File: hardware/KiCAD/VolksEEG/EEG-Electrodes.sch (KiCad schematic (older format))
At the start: 33 parts, among them J1 Conn_02x13_Odd_Even

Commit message: Updating analogue inputs to the referential montage and connected a few ADS1299 pins.
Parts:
- removed C11, C? (x14): 4.7n, Capacitor_SMD:C_0603_1608Metric_Pad1.08x0.95mm_HandSolder, symbol Device:C
- removed R? (x8): 4.99k, Resistor_SMD:R_0603_1608Metric_Pad0.98x0.95mm_HandSolder, symbol Device:R
- added C? (x8): 4.7n, Capacitor_SMD:C_0603_1608Metric_Pad1.08x0.95mm_HandSolder, symbol Device:C
- added R? (x3): 4.99k, Resistor_SMD:R_0603_1608Metric_Pad0.98x0.95mm_HandSolder, symbol Device:R
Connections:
- net labels added: AIN1, AIN2, AIN3, AIN4, AIN5, AIN6, AIN7, AIN8, BIAS_INV, BIAS_OUT, REF
- net labels removed: AIN1N, AIN1P, AIN2N, AIN2P, AIN3N, AIN3P, AIN4N, AIN4P, AIN5N, AIN5P, AIN6N, AIN6P, AIN7N, AIN7P, AIN8N, AIN8P
- wire segments 116 -> 74
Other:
- moved on the sheet: C10, R1, R?

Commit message: Updated names of heirarchical pins, finished referential montage configuration, added filter cap to ADS_nRST line, started putting ADS1299 gpios to a header.
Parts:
- removed J1: Conn_02x13_Odd_Even, Connector_PinHeader_2.54mm:PinHeader_2x13_P2.54mm_Vertical, symbol Connector_Generic:Conn_02x13_Odd_Even
- added J?: Conn_01x10, symbol Connector_Generic:Conn_01x10
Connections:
- net labels removed: ELEC1N, ELEC1P, ELEC2N, ELEC2P, ELEC3N, ELEC3P, ELEC4N, ELEC4P, ELEC5N, ELEC5P, ELEC6N, ELEC6P, ELEC7N, ELEC7P, ELEC8N, ELEC8P, GNDA, VDDA, VSSA
- wire segments 74 -> 76
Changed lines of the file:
@@
 AIN8
-$Comp
-L Connector_Generic:Conn_02x13_Odd_Even J1
-U 1 1 61659FCB
-P 8600 3450
-F 0 "J1" H 8650 2625 50  0000 C CNN
-F 1 "Conn_02x13_Odd_Even" H 8650 2716 50  0000 C CNN
-F 2 "Connector_PinHeader_2.54mm:PinHeader_2x13_P2.54mm_Vertical" H 8600 3450 50  0001 C CNN
-F 3 "~" H 8600 3450 50  0001 C CNN
-	1    8600 3450
-	-1   0    0    1
-$EndComp
-$Comp
-L power:VDDA #PWR036
-U 1 1 6165D31B
-P 7950 2750
-F 0 "#PWR036" H 7950 2600 50  0001 C CNN
-F 1 "VDDA" H 7965 2923 50  0000 C CNN
-F 2 "" H 7950 2750 50  0001 C CNN
-F 3 "" H 7950 2750 50  0001 C CNN
-	1    7950 2750
-	1    0    0    -1
-$EndComp
-$Comp
-L power:VDDA #PWR039
-U 1 1 6165DEAF
-P 9150 2750
-F 0 "#PWR039" H 9150 2600 50  0001 C CNN
-F 1 "VDDA" H 9165 2923 50  0000 C CNN
-F 2 "" H 9150 2750 50  0001 C CNN
-F 3 "" H 9150 2750 50  0001 C CNN
-	1    9150 2750
-	1    0    0    -1
-$EndComp
-$Comp
-L power:VSSA #PWR038
-U 1 1 6165EC47
-P 8800 4150
-F 0 "#PWR038" H 8800 4000 50  0001 C CNN
-F 1 "VSSA" H 8815 4323 50  0000 C CNN
-F 2 "" H 8800 4150 50  0001 C CNN
-F 3 "" H 8800 4150 50  0001 C CNN
-	1    8800 4150
-	-1   0    0    1
-$EndComp
-$Comp
-L power:VSSA #PWR037
-U 1 1 6165FAEA
-P 8300 4150
-F 0 "#PWR037" H 8300 4000 50  0001 C CNN
-F 1 "VSSA" H 8315 4323 50  0000 C CNN
-F 2 "" H 8300 4150 50  0001 C CNN
-F 3 "" H 8300 4150 50  0001 C CNN
-	1    8300 4150
-	-1   0    0    1
-$EndComp
-Wire Wire Line
-	9200 2950 8800 2950
-Wire Wire Line
-	8800 2850 9150 2850
-Wire Wire Line
-	9150 2850 9150 2750
-Wire Wire Line
-	8300 2850 7950 2850
-Wire Wire Line
-	7950 2850 7950 2750
-Wire Wire Line
-	7900 2950 8300 2950
-Wire Wire Line
-	8300 4150 8300 4050
-Wire Wire Line
-	8800 4050 8800 4150
-Wire Wire Line
-	7950 3050 8300 3050
-Wire Wire Line
-	7950 3150 8300 3150
-Wire Wire Line
-	7950 3250 8300 3250
-Wire Wire Line
-	7950 3350 8300 3350
-Wire Wire Line
-	7950 3450 8300 3450
-Wire Wire Line
-	7950 3550 8300 3550
-Wire Wire Line
-	7950 3650 8300 3650
-Wire Wire Line
-	7950 3750 8300 3750
-Wire Wire Line
-	7950 3850 8300 3850
-Wire Wire Line
-	7950 3950 8300 3950
-Wire Wire Line
-	9150 3950 8800 3950
-Wire Wire Line
-	9150 3850 8800 3850
-Wire Wire Line
-	9150 3750 8800 3750
-Wire Wire Line
-	9150 3650 8800 3650
-Wire Wire Line
-	9150 3550 8800 3550
-Wire Wire Line
-	9150 3450 8800 3450
-Wire Wire Line
-	9150 3350 8800 3350
-Wire Wire Line
-	9150 3250 8800 3250
-Wire Wire Line
-	9150 3150 8800 3150
-Wire Wire Line
-	9150 3050 8800 3050
-Text Label 7950 3850 0    50   ~ 0
-ELEC1N
-Text Label 8850 3850 0    50   ~ 0
-ELEC1P
-Entry Wire Line
-	7850 3250 7950 3150
-Entry Wire Line
-	7850 3150 7950 3050
-Entry Wire Line
-	7850 3350 7950 3250
-Entry Wire Line
-	7850 3450 7950 3350
-Entry Wire Line
-	7850 3550 7950 3450
-Entry Wire Line
-	7850 3650 7950 3550
-Entry Wire Line
-	7850 3750 7950 3650
-Entry Wire Line
-	7850 3850 7950 3750
-Entry Wire Line
-	7850 3950 7950 3850
-Entry Wire Line
-	7850 4050 7950 3950
-Entry Wire Line
-	9250 3150 9150 3050
-Entry Wire Line
-	9250 3250 9150 3150
-Entry Wire Line
-	9250 3350 9150 3250
-Entry Wire Line
-	9250 3450 9150 3350
-Entry Wire Line
-	9250 3550 9150 3450
-Entry Wire Line
-	9250 3650 9150 3550
-Entry Wire Line
-	9250 3750 9150 3650
-Entry Wire Line
-	9250 3850 9150 3750
-Entry Wire Line
-	9250 3950 9150 3850
-Entry Wire Line
-	9250 4050 9150 3950
-Text Label 7950 3750 0    50   ~ 0
-ELEC2N
-Text Label 8850 3750 0    50   ~ 0
-ELEC2P
-Text Label 7950 3650 0    50   ~ 0
-ELEC3N
-Text Label 8850 3650 0    50   ~ 0
-ELEC3P
-Text Label 7950 3550 0    50   ~ 0
-ELEC4N
-Text Label 8850 3550 0    50   ~ 0
-ELEC4P
-Text Label 7950 3450 0    50   ~ 0
-ELEC5N
-Text Label 8850 3450 0    50   ~ 0
-ELEC5P
-Text Label 7950 3350 0    50   ~ 0
-ELEC6N
-Text Label 8850 3350 0    50   ~ 0
-ELEC6P
-Text Label 7950 3250 0    50   ~ 0
-ELEC7N
-Text Label 8850 3250 0    50   ~ 0
-ELEC7P
-Text Label 7950 3150 0    50   ~ 0
-ELEC8N
-Text Label 8850 3150 0    50   ~ 0
-ELEC8P
 $Comp
 L Device:R R?
@@
 	1    5800 3950
 	0    1    1    0
-$EndComp
-$Comp
-L power:GNDA #PWR?
-U 1 1 617E796B
-P 7900 2950
-F 0 "#PWR?" H 7900 2700 50  0001 C CNN
-F 1 "GNDA" H 7905 2777 50  0000 C CNN
-F 2 "" H 7900 2950 50  0001 C CNN
-F 3 "" H 7900 2950 50  0001 C CNN
-	1    7900 2950
-	0    1    1    0
-$EndComp
-$Comp
-L power:GNDA #PWR?
-U 1 1 617EC38A
-P 9200 2950
-F 0 "#PWR?" H 9200 2700 50  0001 C CNN
-F 1 "GNDA" H 9205 2777 50  0000 C CNN
-F 2 "" H 9200 2950 50  0001 C CNN
-F 3 "" H 9200 2950 50  0001 C CNN
-	1    9200 2950
-	0    -1   -1   0
 $EndComp
 Text HLabel 2200 4600 0    50   Output ~ 0
@@
 	5650 5200 3100 5200
 Connection ~ 3100 5200
+$Comp
+L Connector_Generic:Conn_01x10 J?
+U 1 1 61B400D9
+P 8500 3150
+F 0 "J?" H 8580 3142 50  0000 L CNN
+F 1 "Conn_01x10" H 8580 3051 50  0000 L CNN
+F 2 "" H 8500 3150 50  0001 C CNN
+F 3 "~" H 8500 3150 50  0001 C CNN
+	1    8500 3150
+	1    0    0    -1
+$EndComp
+Wire Wire Line
+	5950 1850 7750 1850
+Wire Wire Line
+	7750 1850 7750 2750
+Wire Wire Line
+	7750 2750 8300 2750
+Wire Wire Line
+	5950 2150 7600 2150
+Wire Wire Line
+	7600 2150 7600 2850
+Wire Wire Line
+	7600 2850 8300 2850
+Wire Wire Line
+	7450 2950 7450 2450
+Wire Wire Line
+	7450 2450 5950 2450
+Wire Wire Line
+	5950 2750 7300 2750
+Wire Wire Line
+	7300 2750 7300 3050
+Wire Wire Line
+	7300 3050 8300 3050
+Wire Wire Line
+	8300 3150 7150 3150
+Wire Wire Line
+	7150 3150 7150 3050
+Wire Wire Line
+	7150 3050 5950 3050
+Wire Wire Line
+	7450 2950 8300 2950
+Wire Wire Line
+	5950 3350 7150 3350
+Wire Wire Line
+	7150 3350 7150 3250
+Wire Wire Line
+	7150 3250 8300 3250
+Wire Wire Line
+	8300 3350 7300 3350
+Wire Wire Line
+	7300 3650 5950 3650
+Wire Wire Line
+	7300 3350 7300 3650
+Wire Wire Line
+	5950 3950 7450 3950
+Wire Wire Line
+	7450 3950 7450 3450
+Wire Wire Line
+	7450 3450 8300 3450
+Wire Wire Line
+	5950 4600 7600 4600
+Wire Wire Line
+	7600 4600 7600 3550
+Wire Wire Line
+	7600 3550 8300 3550
+Wire Wire Line
+	5950 5200 7750 5200
+Wire Wire Line
+	7750 5200 7750 3650
+Wire Wire Line
+	7750 3650 8300 3650
 $EndSCHEMATC

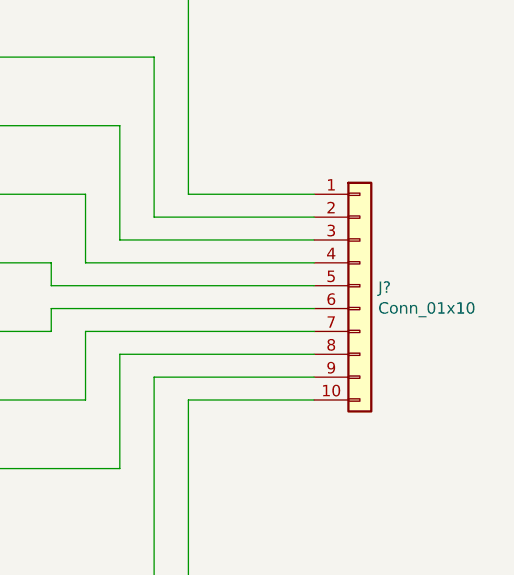
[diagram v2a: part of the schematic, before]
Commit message: Added custom power symbols for non isolated power. Seperated Analogue and digital supplies. finished putting the ADS1299 GPIOs to a header.
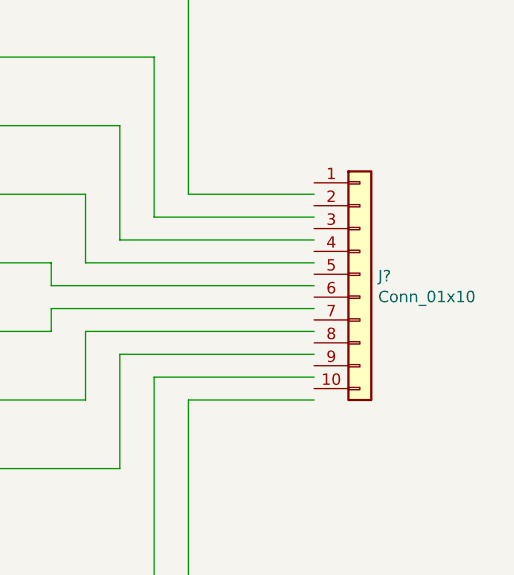
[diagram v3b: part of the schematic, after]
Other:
- moved on the sheet: J?
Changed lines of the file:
@@
 L Connector_Generic:Conn_01x10 J?
 U 1 1 61B400D9
-P 8500 3150
-F 0 "J?" H 8580 3142 50  0000 L CNN
-F 1 "Conn_01x10" H 8580 3051 50  0000 L CNN
-F 2 "" H 8500 3150 50  0001 C CNN
-F 3 "~" H 8500 3150 50  0001 C CNN
-	1    8500 3150
+P 8500 3100
+F 0 "J?" H 8580 3092 50  0000 L CNN
+F 1 "Conn_01x10" H 8580 3001 50  0000 L CNN
+F 2 "" H 8500 3100 50  0001 C CNN
+F 3 "~" H 8500 3100 50  0001 C CNN
+	1    8500 3100
 	1    0    0    -1
 $EndComp

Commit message: Added debugging bits to more schematic sheets.
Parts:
- C10, C? (x8): value 4.7n -> 33n
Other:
- note added: "RC values chosen to give roughly 1KHz -3dB point"
- moved on the sheet: J?
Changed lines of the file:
@@
 $Descr A4 11693 8268
 encoding utf-8
-Sheet 6 6
+Sheet 4 6
 Title ""
 Date ""
@@
 P 2500 4350
 F 0 "C10" H 2615 4396 50  0000 L CNN
-F 1 "4.7n" H 2615 4305 50  0000 L CNN
+F 1 "33n" H 2615 4305 50  0000 L CNN
 F 2 "Capacitor_SMD:C_0603_1608Metric_Pad1.08x0.95mm_HandSolder" H 2538 4200 50  0001 C CNN
 F 3 "~" H 2500 4350 50  0001 C CNN
@@
 P 2900 4350
 F 0 "C?" H 3015 4396 50  0000 L CNN
-F 1 "4.7n" H 3015 4305 50  0000 L CNN
+F 1 "33n" H 3015 4305 50  0000 L CNN
 F 2 "Capacitor_SMD:C_0603_1608Metric_Pad1.08x0.95mm_HandSolder" H 2938 4200 50  0001 C CNN
 F 3 "~" H 2900 4350 50  0001 C CNN
@@
 P 3300 4350
 F 0 "C?" H 3415 4396 50  0000 L CNN
-F 1 "4.7n" H 3415 4305 50  0000 L CNN
+F 1 "33n" H 3415 4305 50  0000 L CNN
 F 2 "Capacitor_SMD:C_0603_1608Metric_Pad1.08x0.95mm_HandSolder" H 3338 4200 50  0001 C CNN
 F 3 "~" H 3300 4350 50  0001 C CNN
@@
 P 3700 4350
 F 0 "C?" H 3815 4396 50  0000 L CNN
-F 1 "4.7n" H 3815 4305 50  0000 L CNN
+F 1 "33n" H 3815 4305 50  0000 L CNN
 F 2 "Capacitor_SMD:C_0603_1608Metric_Pad1.08x0.95mm_HandSolder" H 3738 4200 50  0001 C CNN
 F 3 "~" H 3700 4350 50  0001 C CNN
@@
 P 4100 4350
 F 0 "C?" H 4215 4396 50  0000 L CNN
-F 1 "4.7n" H 4215 4305 50  0000 L CNN
+F 1 "33n" H 4215 4305 50  0000 L CNN
 F 2 "Capacitor_SMD:C_0603_1608Metric_Pad1.08x0.95mm_HandSolder" H 4138 4200 50  0001 C CNN
 F 3 "~" H 4100 4350 50  0001 C CNN
@@
 P 4500 4350
 F 0 "C?" H 4615 4396 50  0000 L CNN
-F 1 "4.7n" H 4615 4305 50  0000 L CNN
+F 1 "33n" H 4615 4305 50  0000 L CNN
 F 2 "Capacitor_SMD:C_0603_1608Metric_Pad1.08x0.95mm_HandSolder" H 4538 4200 50  0001 C CNN
 F 3 "~" H 4500 4350 50  0001 C CNN
@@
 P 4950 4350
 F 0 "C?" H 5065 4396 50  0000 L CNN
-F 1 "4.7n" H 5065 4305 50  0000 L CNN
+F 1 "33n" H 5065 4305 50  0000 L CNN
 F 2 "Capacitor_SMD:C_0603_1608Metric_Pad1.08x0.95mm_HandSolder" H 4988 4200 50  0001 C CNN
 F 3 "~" H 4950 4350 50  0001 C CNN
@@
 P 5350 4350
 F 0 "C?" H 5465 4396 50  0000 L CNN
-F 1 "4.7n" H 5465 4305 50  0000 L CNN
+F 1 "33n" H 5465 4305 50  0000 L CNN
 F 2 "Capacitor_SMD:C_0603_1608Metric_Pad1.08x0.95mm_HandSolder" H 5388 4200 50  0001 C CNN
 F 3 "~" H 5350 4350 50  0001 C CNN
@@
 AR Path="/615BA110/61ADFC6A" Ref="C?"  Part="1"
 F 0 "C?" H 2865 5096 50  0000 L CNN
-F 1 "4.7n" H 2865 5005 50  0000 L CNN
+F 1 "33n" H 2865 5005 50  0000 L CNN
 F 2 "Capacitor_SMD:C_0603_1608Metric_Pad1.08x0.95mm_HandSolder" H 2788 4900 50  0001 C CNN
 F 3 "~" H 2750 5050 50  0001 C CNN
@@
 L Connector_Generic:Conn_01x10 J?
 U 1 1 61B400D9
-P 8500 3100
-F 0 "J?" H 8580 3092 50  0000 L CNN
-F 1 "Conn_01x10" H 8580 3001 50  0000 L CNN
-F 2 "" H 8500 3100 50  0001 C CNN
-F 3 "~" H 8500 3100 50  0001 C CNN
-	1    8500 3100
+P 8500 3150
+F 0 "J?" H 8580 3142 50  0000 L CNN
+F 1 "Conn_01x10" H 8580 3051 50  0000 L CNN
+F 2 "" H 8500 3150 50  0001 C CNN
+F 3 "~" H 8500 3150 50  0001 C CNN
+	1    8500 3150
 	1    0    0    -1
 $EndComp
@@
 Wire Wire Line
 	7750 3650 8300 3650
+Text Notes 3400 1600 0    50   ~ 0
+RC values chosen to give roughly 1KHz -3dB point
 $EndSCHEMATC

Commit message: tweaks to the ADS1299 schematic.
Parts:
- C?: value 33n -> 1.5n
- R?: value 4.99k -> 1M
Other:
- moved on the sheet: C?, R?
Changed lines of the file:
@@
 L Device:R R?
 U 1 1 61ADFC5E
-P 3100 5050
+P 2900 5050
 AR Path="/615BA18D/61ADFC5E" Ref="R?"  Part="1"
 AR Path="/615BA110/61ADFC5E" Ref="R?"  Part="1"
-F 0 "R?" V 2893 5050 50  0000 C CNN
-F 1 "4.99k" V 2984 5050 50  0000 C CNN
-F 2 "Resistor_SMD:R_0603_1608Metric_Pad0.98x0.95mm_HandSolder" V 3030 5050 50  0001 C CNN
-F 3 "~" H 3100 5050 50  0001 C CNN
-	1    3100 5050
+F 0 "R?" V 2693 5050 50  0000 C CNN
+F 1 "1M" V 2784 5050 50  0000 C CNN
+F 2 "Resistor_SMD:R_0603_1608Metric_Pad0.98x0.95mm_HandSolder" V 2830 5050 50  0001 C CNN
+F 3 "~" H 2900 5050 50  0001 C CNN
+	1    2900 5050
 	1    0    0    -1
 $EndComp
@@
 L Device:C C?
 U 1 1 61ADFC6A
-P 2750 5050
+P 3300 5050
 AR Path="/615BA18D/61ADFC6A" Ref="C?"  Part="1"
 AR Path="/615BA110/61ADFC6A" Ref="C?"  Part="1"
-F 0 "C?" H 2865 5096 50  0000 L CNN
-F 1 "33n" H 2865 5005 50  0000 L CNN
-F 2 "Capacitor_SMD:C_0603_1608Metric_Pad1.08x0.95mm_HandSolder" H 2788 4900 50  0001 C CNN
-F 3 "~" H 2750 5050 50  0001 C CNN
-	1    2750 5050
+F 0 "C?" H 3415 5096 50  0000 L CNN
+F 1 "1.5n" H 3415 5005 50  0000 L CNN
+F 2 "Capacitor_SMD:C_0603_1608Metric_Pad1.08x0.95mm_HandSolder" H 3338 4900 50  0001 C CNN
+F 3 "~" H 3300 5050 50  0001 C CNN
+	1    3300 5050
 	-1   0    0    1
 $EndComp
@@
 BIAS_OUT
 Wire Wire Line
-	2200 4900 2750 4900
+	2200 4900 2900 4900
 Wire Wire Line
-	2750 5200 2200 5200
+	3300 5200 2900 5200
 Wire Wire Line
-	2750 4900 3100 4900
-Connection ~ 2750 4900
+	3300 4900 2900 4900
+Connection ~ 3300 5200
 Wire Wire Line
-	3100 5200 2750 5200
-Connection ~ 2750 5200
-Wire Wire Line
-	5650 5200 3100 5200
-Connection ~ 3100 5200
+	5650 5200 3300 5200
+Connection ~ 2900 5200
 $Comp
 L Connector_Generic:Conn_01x10 J?
@@
 Text Notes 3400 1600 0    50   ~ 0
 RC values chosen to give roughly 1KHz -3dB point
+Connection ~ 2900 4900
+Wire Wire Line
+	2900 5200 2200 5200
 $EndSCHEMATC

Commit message: Annotated schematic and cleared ERC errors.
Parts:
- gave numbers to parts that had none: 19
- renumbered C10 to C7, R1 to R21
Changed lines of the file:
@@
 $Descr A4 11693 8268
 encoding utf-8
-Sheet 4 6
+Sheet 3 6
 Title ""
 Date ""
@@
 $EndDescr
 $Comp
-L Device:R R1
+L Device:R R21
 U 1 1 615BC506
 P 5800 1850
-F 0 "R1" V 5593 1850 50  0000 C CNN
+F 0 "R21" V 5593 1850 50  0000 C CNN
 F 1 "4.99k" V 5684 1850 50  0000 C CNN
 F 2 "Resistor_SMD:R_0603_1608Metric_Pad0.98x0.95mm_HandSolder" V 5730 1850 50  0001 C CNN
@@
 $EndComp
 $Comp
-L Device:C C10
+L Device:C C7
 U 1 1 615BE4A6
 P 2500 4350
-F 0 "C10" H 2615 4396 50  0000 L CNN
+F 0 "C7" H 2615 4396 50  0000 L CNN
 F 1 "33n" H 2615 4305 50  0000 L CNN
 F 2 "Capacitor_SMD:C_0603_1608Metric_Pad1.08x0.95mm_HandSolder" H 2538 4200 50  0001 C CNN
@@
 AIN8
 $Comp
-L Device:R R?
+L Device:R R22
 U 1 1 6167497C
 P 5800 2150
-F 0 "R?" V 5593 2150 50  0000 C CNN
+F 0 "R22" V 5593 2150 50  0000 C CNN
 F 1 "4.99k" V 5684 2150 50  0000 C CNN
 F 2 "Resistor_SMD:R_0603_1608Metric_Pad0.98x0.95mm_HandSolder" V 5730 2150 50  0001 C CNN
@@
 $EndComp
 $Comp
-L Device:R R?
+L Device:R R23
 U 1 1 616792D7
 P 5800 2450
-F 0 "R?" V 5593 2450 50  0000 C CNN
+F 0 "R23" V 5593 2450 50  0000 C CNN
 F 1 "4.99k" V 5684 2450 50  0000 C CNN
 F 2 "Resistor_SMD:R_0603_1608Metric_Pad0.98x0.95mm_HandSolder" V 5730 2450 50  0001 C CNN
@@
 $EndComp
 $Comp
-L Device:R R?
+L Device:R R25
 U 1 1 616823F5
 P 5800 3050
-F 0 "R?" V 5593 3050 50  0000 C CNN
+F 0 "R25" V 5593 3050 50  0000 C CNN
 F 1 "4.99k" V 5684 3050 50  0000 C CNN
 F 2 "Resistor_SMD:R_0603_1608Metric_Pad0.98x0.95mm_HandSolder" V 5730 3050 50  0001 C CNN
@@
 $EndComp
 $Comp
-L Device:R R?
+L Device:R R24
 U 1 1 61686D5D
 P 5800 2750
-F 0 "R?" V 5593 2750 50  0000 C CNN
+F 0 "R24" V 5593 2750 50  0000 C CNN
 F 1 "4.99k" V 5684 2750 50  0000 C CNN
 F 2 "Resistor_SMD:R_0603_1608Metric_Pad0.98x0.95mm_HandSolder" V 5730 2750 50  0001 C CNN
@@
 $EndComp
 $Comp
-L Device:R R?
+L Device:R R26
 U 1 1 61690CA9
 P 5800 3350
-F 0 "R?" V 5593 3350 50  0000 C CNN
+F 0 "R26" V 5593 3350 50  0000 C CNN
 F 1 "4.99k" V 5684 3350 50  0000 C CNN
 F 2 "Resistor_SMD:R_0603_1608Metric_Pad0.98x0.95mm_HandSolder" V 5730 3350 50  0001 C CNN
@@
 $EndComp
 $Comp
-L Device:R R?
+L Device:R R27
 U 1 1 616955F3
 P 5800 3650
-F 0 "R?" V 5593 3650 50  0000 C CNN
+F 0 "R27" V 5593 3650 50  0000 C CNN
 F 1 "4.99k" V 5684 3650 50  0000 C CNN
 F 2 "Resistor_SMD:R_0603_1608Metric_Pad0.98x0.95mm_HandSolder" V 5730 3650 50  0001 C CNN
@@
 $EndComp
 $Comp
-L Device:R R?
+L Device:R R28
 U 1 1 616BEE2C
 P 5800 3950
-F 0 "R?" V 5593 3950 50  0000 C CNN
+F 0 "R28" V 5593 3950 50  0000 C CNN
 F 1 "4.99k" V 5684 3950 50  0000 C CNN
 F 2 "Resistor_SMD:R_0603_1608Metric_Pad0.98x0.95mm_HandSolder" V 5730 3950 50  0001 C CNN
@@
 BIAS_INV
 $Comp
-L Device:C C?
+L Device:C C8
 U 1 1 61AB19F6
 P 2900 4350
-F 0 "C?" H 3015 4396 50  0000 L CNN
+F 0 "C8" H 3015 4396 50  0000 L CNN
 F 1 "33n" H 3015 4305 50  0000 L CNN
 F 2 "Capacitor_SMD:C_0603_1608Metric_Pad1.08x0.95mm_HandSolder" H 2938 4200 50  0001 C CNN
@@
 $EndComp
 $Comp
-L Device:C C?
+L Device:C C9
 U 1 1 61AB1D05
 P 3300 4350
-F 0 "C?" H 3415 4396 50  0000 L CNN
+F 0 "C9" H 3415 4396 50  0000 L CNN
 F 1 "33n" H 3415 4305 50  0000 L CNN
 F 2 "Capacitor_SMD:C_0603_1608Metric_Pad1.08x0.95mm_HandSolder" H 3338 4200 50  0001 C CNN
@@
 $EndComp
 $Comp
-L Device:C C?
+L Device:C C11
 U 1 1 61AB1FA5
 P 3700 4350
-F 0 "C?" H 3815 4396 50  0000 L CNN
+F 0 "C11" H 3815 4396 50  0000 L CNN
 F 1 "33n" H 3815 4305 50  0000 L CNN
 F 2 "Capacitor_SMD:C_0603_1608Metric_Pad1.08x0.95mm_HandSolder" H 3738 4200 50  0001 C CNN
@@
 $EndComp
 $Comp
-L Device:C C?
+L Device:C C12
 U 1 1 61AB22D6
 P 4100 4350
-F 0 "C?" H 4215 4396 50  0000 L CNN
+F 0 "C12" H 4215 4396 50  0000 L CNN
 F 1 "33n" H 4215 4305 50  0000 L CNN
 F 2 "Capacitor_SMD:C_0603_1608Metric_Pad1.08x0.95mm_HandSolder" H 4138 4200 50  0001 C CNN
@@
 $EndComp
 $Comp
-L Device:C C?
+L Device:C C13
 U 1 1 61AB2629
 P 4500 4350
-F 0 "C?" H 4615 4396 50  0000 L CNN
+F 0 "C13" H 4615 4396 50  0000 L CNN
 F 1 "33n" H 4615 4305 50  0000 L CNN
 F 2 "Capacitor_SMD:C_0603_1608Metric_Pad1.08x0.95mm_HandSolder" H 4538 4200 50  0001 C CNN
@@
 $EndComp
 $Comp
-L Device:C C?
+L Device:C C14
 U 1 1 61AB27FD
 P 4950 4350
-F 0 "C?" H 5065 4396 50  0000 L CNN
+F 0 "C14" H 5065 4396 50  0000 L CNN
 F 1 "33n" H 5065 4305 50  0000 L CNN
 F 2 "Capacitor_SMD:C_0603_1608Metric_Pad1.08x0.95mm_HandSolder" H 4988 4200 50  0001 C CNN
@@
 $EndComp
 $Comp
-L Device:C C?
+L Device:C C15
 U 1 1 61AB2A6A
 P 5350 4350
-F 0 "C?" H 5465 4396 50  0000 L CNN
+F 0 "C15" H 5465 4396 50  0000 L CNN
 F 1 "33n" H 5465 4305 50  0000 L CNN
 F 2 "Capacitor_SMD:C_0603_1608Metric_Pad1.08x0.95mm_HandSolder" H 5388 4200 50  0001 C CNN
@@
 	5650 3950 2500 3950
 $Comp
-L Device:R R?
+L Device:R R29
 U 1 1 61ABA7AA
 P 5800 4600
-F 0 "R?" V 5593 4600 50  0000 C CNN
+F 0 "R29" V 5593 4600 50  0000 C CNN
 F 1 "4.99k" V 5684 4600 50  0000 C CNN
 F 2 "Resistor_SMD:R_0603_1608Metric_Pad0.98x0.95mm_HandSolder" V 5730 4600 50  0001 C CNN
@@
 	5350 1850 5650 1850
 $Comp
-L Device:R R?
+L Device:R R20
 U 1 1 61ADFC5E
 P 2900 5050
-AR Path="/615BA18D/61ADFC5E" Ref="R?"  Part="1"
+AR Path="/615BA18D/61ADFC5E" Ref="R20"  Part="1"
 AR Path="/615BA110/61ADFC5E" Ref="R?"  Part="1"
-F 0 "R?" V 2693 5050 50  0000 C CNN
+F 0 "R20" V 2693 5050 50  0000 C CNN
 F 1 "1M" V 2784 5050 50  0000 C CNN
 F 2 "Resistor_SMD:R_0603_1608Metric_Pad0.98x0.95mm_HandSolder" V 2830 5050 50  0001 C CNN
@@
 $EndComp
 $Comp
-L Device:R R?
+L Device:R R30
 U 1 1 61ADFC64
 P 5800 5200
-AR Path="/615BA18D/61ADFC64" Ref="R?"  Part="1"
+AR Path="/615BA18D/61ADFC64" Ref="R30"  Part="1"
 AR Path="/615BA110/61ADFC64" Ref="R?"  Part="1"
-F 0 "R?" V 5593 5200 50  0000 C CNN
+F 0 "R30" V 5593 5200 50  0000 C CNN
 F 1 "4.99k" V 5684 5200 50  0000 C CNN
 F 2 "Resistor_SMD:R_0603_1608Metric_Pad0.98x0.95mm_HandSolder" V 5730 5200 50  0001 C CNN
@@
 $EndComp
 $Comp
-L Device:C C?
+L Device:C C10
 U 1 1 61ADFC6A
 P 3300 5050
-AR Path="/615BA18D/61ADFC6A" Ref="C?"  Part="1"
+AR Path="/615BA18D/61ADFC6A" Ref="C10"  Part="1"
 AR Path="/615BA110/61ADFC6A" Ref="C?"  Part="1"
-F 0 "C?" H 3415 5096 50  0000 L CNN
+F 0 "C10" H 3415 5096 50  0000 L CNN
 F 1 "1.5n" H 3415 5005 50  0000 L CNN
 F 2 "Capacitor_SMD:C_0603_1608Metric_Pad1.08x0.95mm_HandSolder" H 3338 4900 50  0001 C CNN
@@
 Connection ~ 2900 5200
 $Comp
-L Connector_Generic:Conn_01x10 J?
+L Connector_Generic:Conn_01x10 J4
 U 1 1 61B400D9
 P 8500 3150
-F 0 "J?" H 8580 3142 50  0000 L CNN
+F 0 "J4" H 8580 3142 50  0000 L CNN
 F 1 "Conn_01x10" H 8580 3051 50  0000 L CNN
 F 2 "" H 8500 3150 50  0001 C CNN
